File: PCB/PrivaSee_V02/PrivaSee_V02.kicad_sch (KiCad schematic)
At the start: 26 parts, among them J1 RFPC-SMA27-F, J2 Batt_Solder_Point, J3 Conn_02x06_Odd_Even, SW1 (Generic toggle state switch), U1 RC1602A, U2 LM358, U3 254, U4 DFR0568, U6 ESP32-C5-DevKitC-1

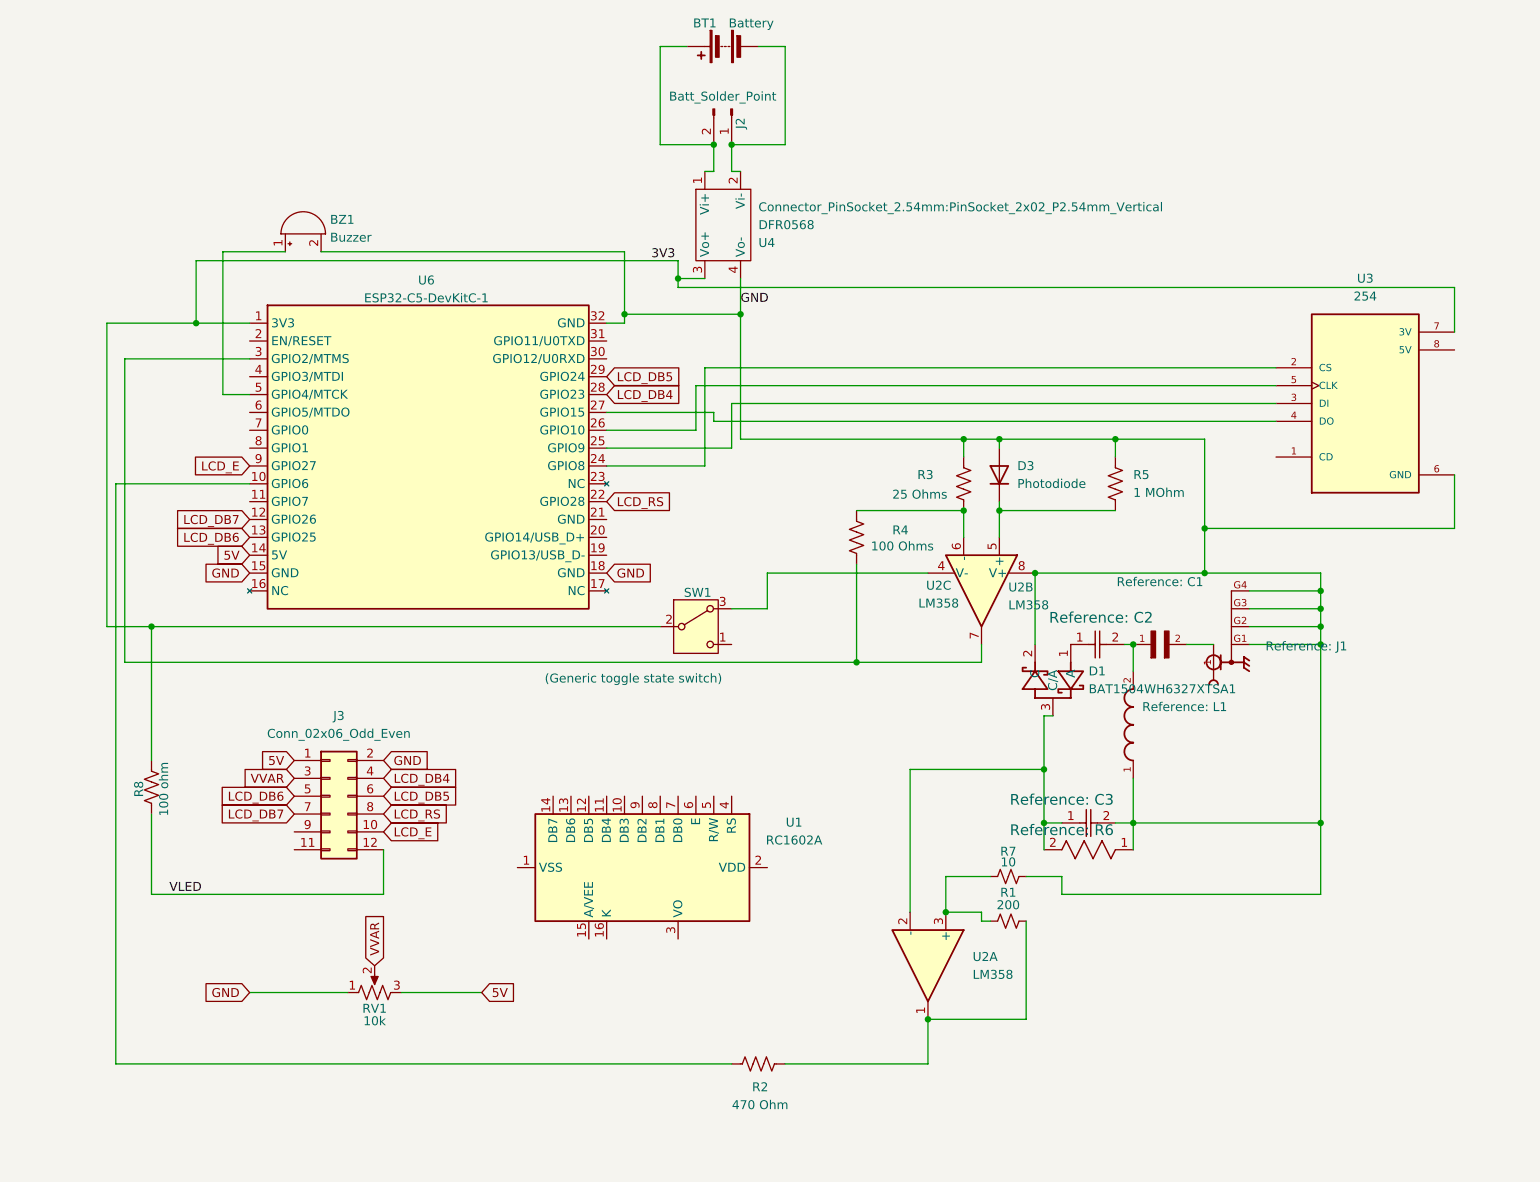
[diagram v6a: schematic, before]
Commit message: PCB Updates
Added a button, changed switch functionality, and added holes for the mounting of the board.
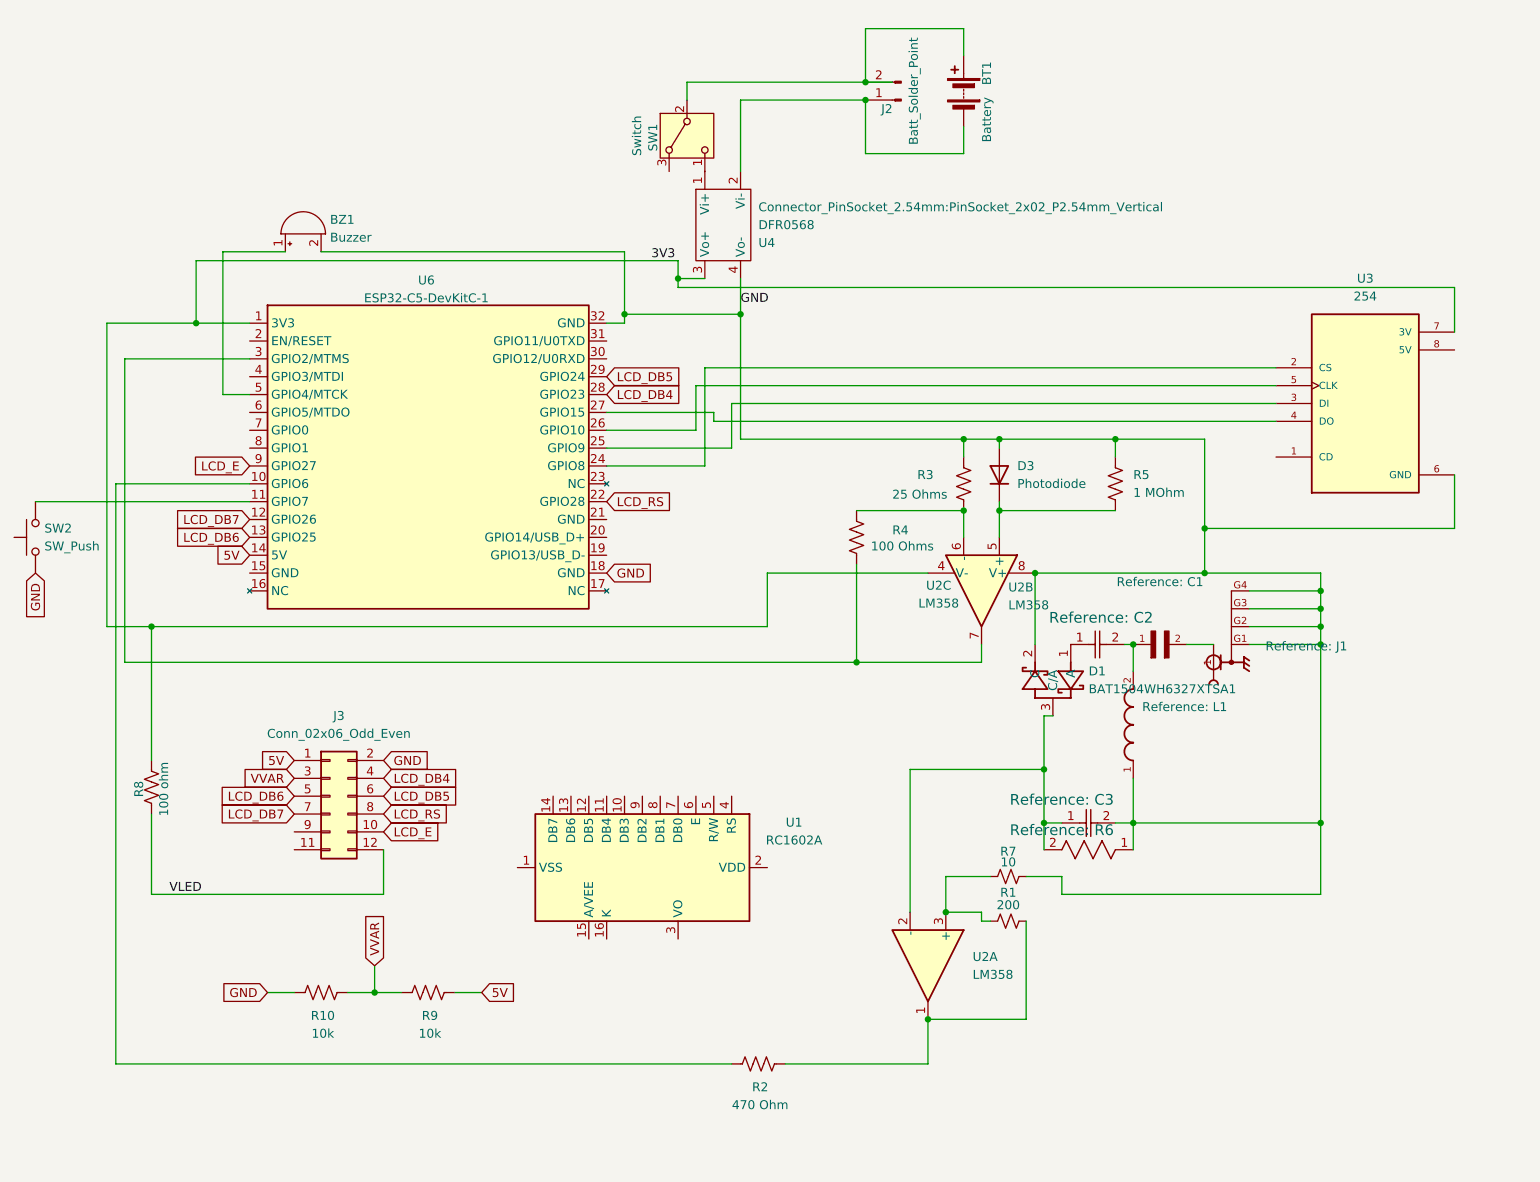
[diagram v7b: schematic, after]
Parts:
- removed RV1: 10k, Potentiometer_THT:Potentiometer_ACP_CA6-H2,5_Horizontal, symbol Device:R_Potentiometer_US
- added R10, R9: 10k, Resistor_SMD:R_1206_3216Metric_Pad1.30x1.75mm_HandSolder, symbol Device:R_US
- added SW2: SW_Push, Button_Switch_THT:SW_PUSH_6mm_H4.3mm, symbol Switch:SW_Push
- SW1: value (Generic toggle state switch) -> Switch
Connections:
- net 3V3: now also U2.4 (V-); no longer SW1.2 (B)
- net 5V: now also R9.2
- net GND: now also R10.1, SW2.1; no longer U6.15 (GND)
- net VVAR: now also R10.2, R9.1
- net at U6.11 (GPIO7): now also SW2.2
- net at SW1.3 (A): no longer U2.4 (V-)
- net at BT1.1 (+), J2.2 (Batt+): now also SW1.2 (B); no longer U4.1 (Vi+)
- net at SW1.1 (C): now also U4.1 (Vi+)
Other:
- moved on the sheet: BT1, J2
